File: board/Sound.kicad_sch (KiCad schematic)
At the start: 28 parts, among them IC9 LF353P, J29 Audio In 6, J9 SND CT1/2, U38 YM2151, U41 YM3012, U42 TL074

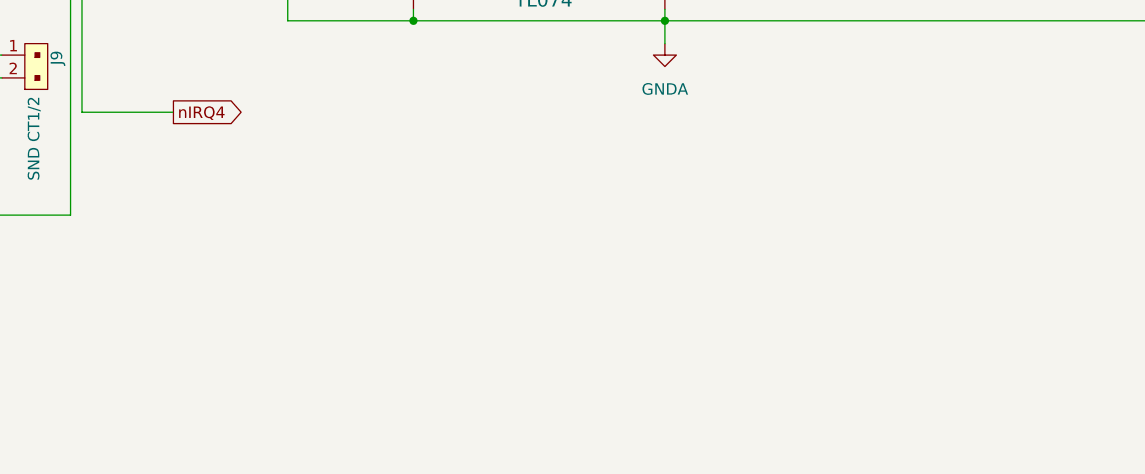
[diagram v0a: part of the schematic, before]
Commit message: Board V1.8D: reliability changes only, the same software as 1.8C
CMOS highs into the W65C02S: U11 (its clock), U22 (IRQB) and U59 (its data bus) are 74ACT parts.
Decoupling at the sound chips and op-amps; four 47 uF bulk capacitors on +5 V; GNDA joined to GND once,
by the YM3012 (R29). Series terminations on the clocks (R23-R27, each driver's net X_SRC) and on the
crystal's drive (R22). A fixed pull-up on RDY (R28); pull-ups on the data bus (RN4: an empty slot reads
$FF). U26's spare half placed and disabled, and U22's spare inputs tied low. ATX pin 20 feeds the slots'
-5V. The ACIA's CTS through a jumper (J30: 1-2 as 1.8C, 2-3 always on). Loose wires removed, no-connects
marked, the root sheet's boxes tidied, and every sheet's revision set to 1.8D. The netlist differs from
1.8C's only by these (checked net by net); ERC finds nothing new. board/CHANGES-1.8D.md lists them. The
PCB isn't updated yet.

Co-Authored-By: Claude Opus 5.5 <noreply@anthropic.com>
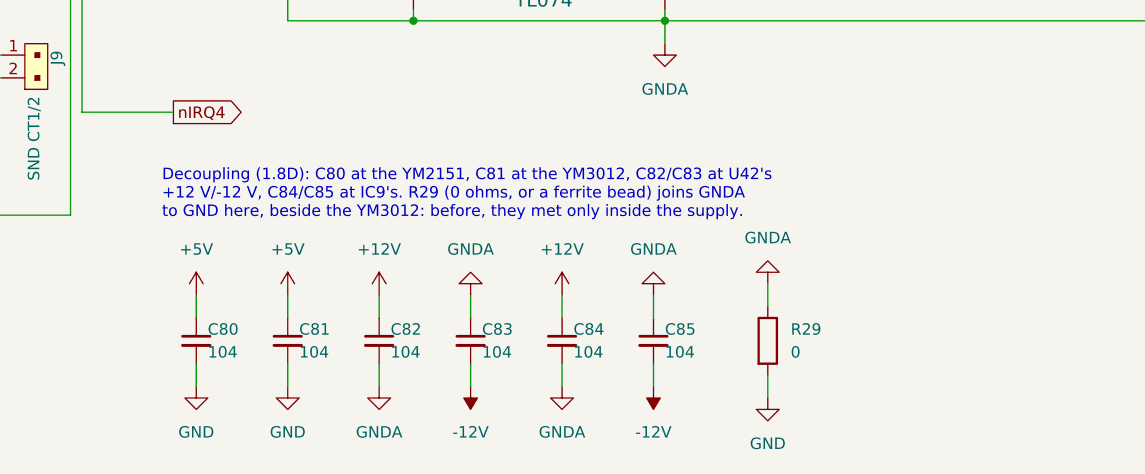
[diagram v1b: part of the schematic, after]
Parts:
- added C80, C81, C82, C83, C84, C85: 104, Capacitor_THT:C_Disc_D5.0mm_W2.5mm_P5.00mm, symbol Device:C_Small
- added R29: 0, Resistor_THT:R_Axial_DIN0207_L6.3mm_D2.5mm_P10.16mm_Horizontal, symbol Device:R
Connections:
- net +12V: now also C82.1, C84.1
- net +5V: now also C80.1, C81.1
- net -12V: now also C83.2, C85.2
- net GND: now also C80.2, C81.2, R29.2
- net GNDA: now also C82.2, C83.1, C84.2, C85.1, R29.1
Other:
- note added: "Decoupling (1.8D): C80 at the YM2151, C81 at the YM3012, C82/C83 at U42's +12 V/-12 V, C84/C85 at IC9's. R29 (0 ohms, or a ferrite bead) joins GNDA to GND here, beside the YM3012: before, they met only inside the supply."
